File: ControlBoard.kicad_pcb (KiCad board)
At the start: 2 copper layers, 60 x 60 mm, 41 parts, among them J1 Conn_02x07_Odd_Even, J2 Conn_02x07_Odd_Even, J3 Conn_02x03_Odd_Even, J5 Conn_01x06, J6 Conn_01x06, J7 Conn_01x02, U1 STM32G473RCTx, U2 AT24CS02-XHM, U3 ICM-42668-P, U4 RT9013-33GB, U6 TLE9251VSJ

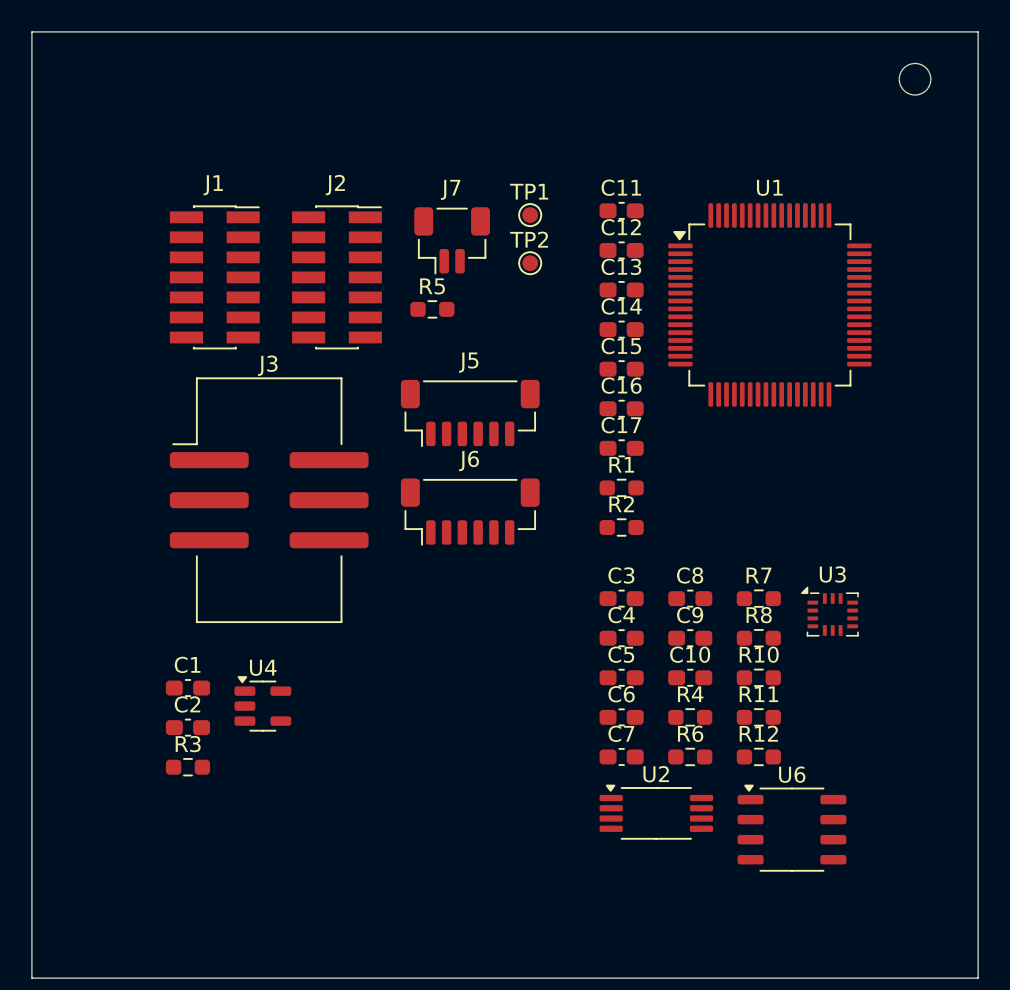
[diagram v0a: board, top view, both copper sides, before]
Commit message: 重新分配端子封装
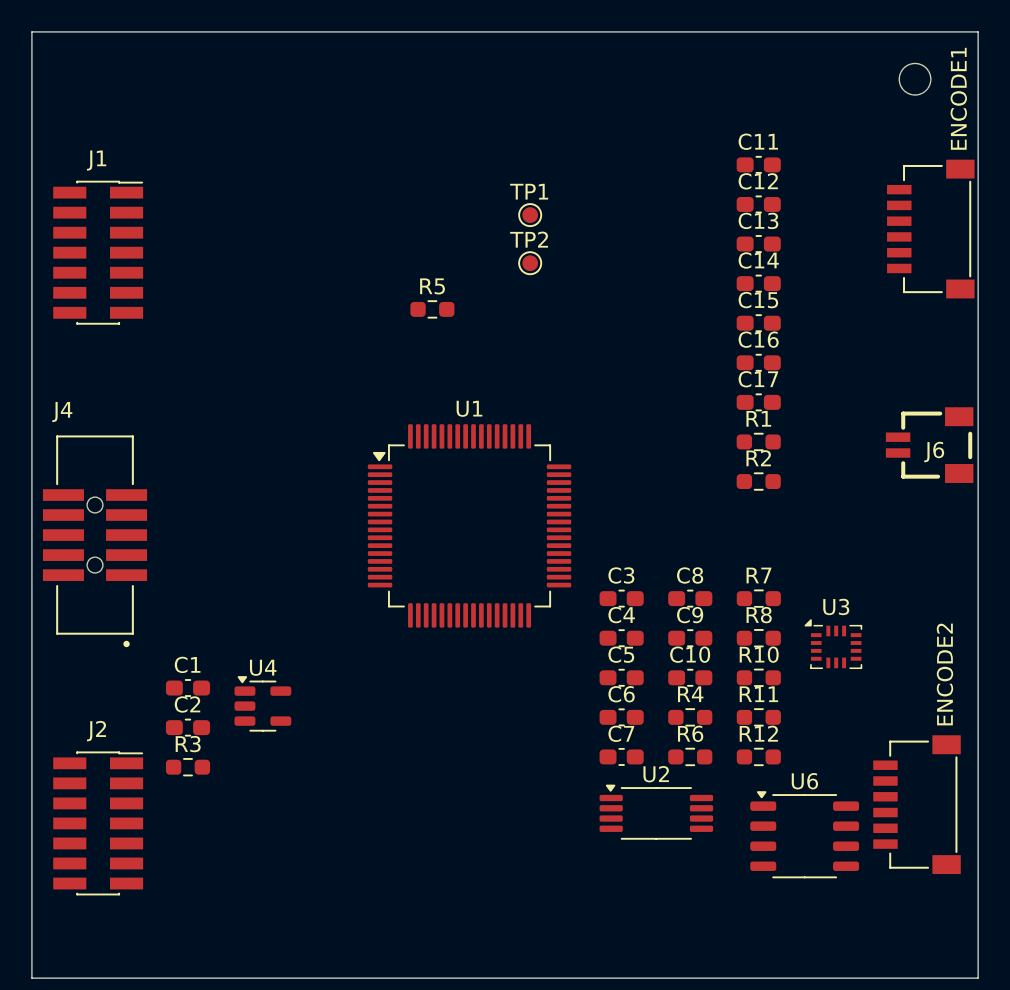
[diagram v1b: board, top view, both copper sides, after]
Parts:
- removed J3: Conn_02x03_Odd_Even, Connector_IDC:IDC-Header_2x03_P2.54mm_Vertical_SMD
- removed J5: Conn_01x06, Connector_JST:JST_SH_BM06B-SRSS-TB_1x06-1MP_P1.00mm_Vertical
- removed J7: Conn_01x02, Connector_JST:JST_SH_BM02B-SRSS-TB_1x02-1MP_P1.00mm_Vertical
- added ENCODE1: ENCODE1, footprints:JST_SH_BM06B-SRSS-TB_1x06-1MP_P1.00mm_Horizontal, F.Cu at (215.0, 70.5)
- added ENCODE2: Conn_01x06_MountingPin, footprints:JST_SH_BM06B-SRSS-TB_1x06-1MP_P1.00mm_Horizontal, F.Cu at (214.1, 107.0)
- added J4: Conn_02x05_Odd_Even, footprints:Box_Head_1.27mm_SMD_Vertical_02x05, F.Cu at (164.0, 89.9)
- J6: value Conn_01x06 -> Conn_01x02_MountingPin; footprint Connector_JST:JST_SH_BM06B-SRSS-TB_1x06-1MP_P1.00mm_Vertical -> footprints:JST_SH_BM02B-SRSS-TB_1x02-1MP_P1.00mm_Horizontal
- moved J2 37.8 mm to (164.2, 108.2)
- moved J6 29.4 mm to (216.9, 84.2), turned to 90 degrees
- moved U1 23.6 mm to (187.8, 89.3)
- moved C12 9.17 mm to (206.1, 68.9)
- moved C14 9.17 mm to (206.1, 74.0)
- moved C15 9.17 mm to (206.1, 76.5)
- moved C17 9.17 mm to (206.1, 81.5)
- moved R1 9.17 mm to (206.1, 84.0)
- moved C11 9.17 mm to (206.1, 66.4)
- moved C13 9.17 mm to (206.1, 71.5)
- moved C16 9.17 mm to (206.1, 79.0)
- moved R2 9.17 mm to (206.1, 86.5)
- moved J1 7.56 mm to (164.2, 72.0)
- moved U3 2.07 mm to (211.0, 97.0)
- moved U6 0.91 mm to (209.0, 109.0)
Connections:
- J6 pad 1: /3.3V -> /CAN_H
- J6 pad 2: /SPI3_CLK -> /CAN_L
- J6 pad MP: (no net) -> GND
- U1 pad 18: /SPI1_CS -> /MOTOR1_ENCODE_CS
- U1 pad 19: /SPI1_CLK -> /MOTOR1_ENCODE_CLK
- U1 pad 20: /SPI1_MISO -> /MOTOR1_ENCODE_MISO
- U1 pad 21: /SPI1_MOSI -> /MOTOR1_ENCODE_MOSI
- U1 pad 51: /SPI3_CS -> /MOTOR2_ENCODE_CS
- U1 pad 52: /SPI3_CLK -> /MOTOR2_ENCODE_CLK
- U1 pad 53: /SPI3_MISO -> /MOTOR2_ENCODE_MISO
- U1 pad 54: /SPI3_MOSI -> /MOTOR2_ENCODE_MOSI

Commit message: 修改板框
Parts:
- moved J2 91.9 mm to (73.0, 97.0)
- moved J4 91.3 mm to (73.0, 82.0)
- moved J1 91.3 mm to (73.0, 67.0)
- moved C1 76.9 mm to (93.1, 94.8)
- moved C2 76.9 mm to (93.1, 97.3)
- moved C3 76.9 mm to (120.6, 89.1)
- moved C4 76.9 mm to (120.6, 91.6)
- moved C5 76.9 mm to (120.6, 94.1)
- moved C6 76.9 mm to (120.6, 96.6)
- moved C7 76.9 mm to (120.6, 99.2)
- moved R3 76.9 mm to (93.1, 99.8)
- moved R5 76.9 mm to (108.6, 70.8)
- moved U4 76.9 mm to (97.9, 95.9)
- moved C10 76.9 mm to (125.0, 94.1)
- moved C11 76.9 mm to (129.3, 61.6)
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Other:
- board size 60 x 60 mm -> 80 x 60 mm

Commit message: PCB初布局
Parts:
- added C18: 22pF, Capacitor_SMD:C_0603_1608Metric_Pad1.08x0.95mm_HandSolder, F.Cu at (120.4, 85.6)
- added C19: 22pF, Capacitor_SMD:C_0603_1608Metric_Pad1.08x0.95mm_HandSolder, F.Cu at (120.1, 81.5)
- added C20: 0.1uF, Capacitor_SMD:C_0603_1608Metric_Pad1.08x0.95mm_HandSolder, F.Cu at (120.4, 75.2)
- added R9: 10K, Resistor_SMD:R_0603_1608Metric_Pad0.98x0.95mm_HandSolder, F.Cu at (118.8, 75.2)
- added SW1: SW_Push, Button_Switch_SMD:SW_SPST_CK_RS282G05A3, F.Cu at (127.0, 74.9)
- added Y1: 12MHz, Crystal:Crystal_SMD_3225-4Pin_3.2x2.5mm, F.Cu at (118.1, 83.6)
- moved C13 40.5 mm to (94.7, 87.7), turned to -90 degrees
- moved ENCODE2 34.5 mm to (142.8, 68.1)
- moved TP1 32.2 mm to (90.0, 85.3), turned to 180 degrees
- moved ENCODE1 30.7 mm to (142.8, 96.0)
- moved U3 29.5 mm to (105.7, 99.6)
- moved TP2 28.7 mm to (90.0, 82.3), turned to 180 degrees
- moved C12 28.4 mm to (101.6, 70.0)
- moved R5 26.7 mm to (84.5, 82.0), turned to 180 degrees
- moved C16 26.6 mm to (109.0, 91.2)
- moved C17 25.2 mm to (105.0, 70.0)
- moved R1 24.5 mm to (109.0, 92.8), turned to 180 degrees
- moved C15 24.3 mm to (105.0, 71.5)
- moved C14 24.1 mm to (113.2, 87.0), turned to -90 degrees
- moved R2 23.9 mm to (109.0, 94.3), turned to 180 degrees
- moved U6 22.2 mm to (131.3, 82.0)
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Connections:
- U1 pad 5: unconnected-(U1-PF0-Pad5) -> Net-(U1-PF0)
- U1 pad 6: unconnected-(U1-PF1-Pad6) -> Net-(U1-PF1)
- U1 pad 7: unconnected-(U1-PG10-Pad7) -> Net-(U1-PG10)
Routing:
- net Net-(U1-PF1): track 0.00 -> 11.0 mm
- net Net-(U3-AP_CS): track 0.00 -> 11.0 mm
- net Net-(U1-PF0): track 0.00 -> 11.0 mm
- net /MCU_Part/Peripheral/24C02_SDA: track 0.00 -> 8.45 mm
- net /MCU_Part/Peripheral/24C02_SCL: track 0.00 -> 6.54 mm
- net Net-(U6-STB): track 0.00 -> 3.54 mm
- net Net-(U2-WP): track 0.00 -> 3.24 mm
- net /MCU_Part/Peripheral/PB6_FDCAN2_TX: track 0.00 -> 3.17 mm
- net Net-(U6-CAN_H): track 0.00 -> 2.93 mm
- net /MCU_Part/Peripheral/PB11_FDCAN2_RX: track 0.00 -> 2.87 mm
- net Net-(U6-CAN_L): track 0.00 -> 2.82 mm
- net Net-(U3-INT2/FSYNC/CLKIN): track 0.00 -> 2.75 mm
- net /CAN_L: track 0.00 -> 2.20 mm
- net /CAN_H: track 0.00 -> 2.20 mm

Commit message: 增加测试点
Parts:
- added TP10: TestPoint_Small, TestPoint:TestPoint_Pad_D1.0mm, F.Cu at (156.2, 87.4)
- added TP11: TestPoint_Small, TestPoint:TestPoint_Pad_D1.0mm, F.Cu at (156.2, 90.4)
- added TP12: TestPoint_Small, TestPoint:TestPoint_Pad_D1.0mm, F.Cu at (156.2, 93.5)
- added TP13: TestPoint_Small, TestPoint:TestPoint_Pad_D1.0mm, F.Cu at (159.3, 72.1)
- added TP14: TestPoint_Small, TestPoint:TestPoint_Pad_D1.0mm, F.Cu at (159.3, 75.2)
- added TP15: TestPoint_Small, TestPoint:TestPoint_Pad_D1.0mm, F.Cu at (159.3, 78.2)
- added TP16: TestPoint_Small, TestPoint:TestPoint_Pad_D1.0mm, F.Cu at (159.3, 81.3)
- added TP17: TestPoint_Small, TestPoint:TestPoint_Pad_D1.0mm, F.Cu at (159.3, 84.3)
- added TP18: TestPoint_Small, TestPoint:TestPoint_Pad_D1.0mm, F.Cu at (159.3, 87.4)
- added TP19: TestPoint_Small, TestPoint:TestPoint_Pad_D1.0mm, F.Cu at (159.3, 90.4)
- added TP20: TestPoint_Small, TestPoint:TestPoint_Pad_D1.0mm, F.Cu at (159.3, 93.5)
- added TP21: TestPoint_Small, TestPoint:TestPoint_Pad_D1.0mm, F.Cu at (162.3, 72.1)
- added TP22: TestPoint_Small, TestPoint:TestPoint_Pad_D1.0mm, F.Cu at (162.3, 75.2)
- added TP23: TestPoint_Small, TestPoint:TestPoint_Pad_D1.0mm, F.Cu at (162.3, 78.2)
- added TP24: TestPoint_Small, TestPoint:TestPoint_Pad_D1.0mm, F.Cu at (162.3, 81.3)
- added TP25: TestPoint_Small, TestPoint:TestPoint_Pad_D1.0mm, F.Cu at (162.3, 84.3)
- added TP26: TestPoint_Small, TestPoint:TestPoint_Pad_D1.0mm, B.Cu at (93.3, 79.3)
- added TP27: TestPoint_Small, TestPoint:TestPoint_Pad_D1.0mm, F.Cu at (162.3, 90.4)
- added TP28: TestPoint_Small, TestPoint:TestPoint_Pad_D1.0mm, F.Cu at (162.3, 93.5)
- added TP29: TestPoint_Small, TestPoint:TestPoint_Pad_D1.0mm, F.Cu at (165.4, 72.1)
- added TP3: TestPoint_Small, TestPoint:TestPoint_Pad_D1.0mm, F.Cu at (140.7, 78.4)
- added TP30: TestPoint_Small, TestPoint:TestPoint_Pad_D1.0mm, F.Cu at (165.4, 75.2)
- added TP31: TestPoint_Small, TestPoint:TestPoint_Pad_D1.0mm, F.Cu at (165.4, 78.2)
- added TP32: TestPoint_Small, TestPoint:TestPoint_Pad_D1.0mm, F.Cu at (165.4, 81.3)
- added TP33: TestPoint_Small, TestPoint:TestPoint_Pad_D1.0mm, F.Cu at (165.4, 84.3)
- added TP34: TestPoint_Small, TestPoint:TestPoint_Pad_D1.0mm, F.Cu at (165.4, 87.4)
- added TP35: TestPoint_Small, TestPoint:TestPoint_Pad_D1.0mm, F.Cu at (165.4, 90.4)
- added TP36: TestPoint_Small, TestPoint:TestPoint_Pad_D1.0mm, F.Cu at (165.4, 93.5)
- added TP37: TestPoint_Small, TestPoint:TestPoint_Pad_D1.0mm, F.Cu at (168.4, 72.1)
- added TP38: TestPoint_Small, TestPoint:TestPoint_Pad_D1.0mm, F.Cu at (168.4, 75.2)
- added TP39: TestPoint_Small, TestPoint:TestPoint_Pad_D1.0mm, F.Cu at (168.4, 78.2)
- added TP4: TestPoint_Small, TestPoint:TestPoint_Pad_D1.0mm, F.Cu at (140.7, 86.6)
- added TP40: TestPoint_Small, TestPoint:TestPoint_Pad_D1.0mm, F.Cu at (168.4, 81.3)
- added TP41: TestPoint_Small, TestPoint:TestPoint_Pad_D1.0mm, F.Cu at (168.4, 84.3)
- added TP42: TestPoint_Small, TestPoint:TestPoint_Pad_D1.0mm, F.Cu at (168.4, 87.4)
- added TP43: TestPoint_Small, TestPoint:TestPoint_Pad_D1.0mm, F.Cu at (168.4, 90.4)
- added TP44: TestPoint_Small, TestPoint:TestPoint_Pad_D1.0mm, F.Cu at (168.4, 93.5)
- added TP45: TestPoint_Small, TestPoint:TestPoint_Pad_D1.0mm, F.Cu at (171.5, 72.1)
- added TP46: TestPoint_Small, TestPoint:TestPoint_Pad_D1.0mm, F.Cu at (171.5, 75.2)
- added TP47: TestPoint_Small, TestPoint:TestPoint_Pad_D1.0mm, F.Cu at (171.5, 78.2)
- added TP48: TestPoint_Small, TestPoint:TestPoint_Pad_D1.0mm, F.Cu at (171.5, 81.3)
- added TP5: TestPoint_Small, TestPoint:TestPoint_Pad_D1.0mm, F.Cu at (156.2, 72.1)
- added TP6: TestPoint_Small, TestPoint:TestPoint_Pad_D1.0mm, F.Cu at (156.2, 75.2)
- added TP7: TestPoint_Small, TestPoint:TestPoint_Pad_D1.0mm, F.Cu at (156.2, 78.2)
- added TP8: TestPoint_Small, TestPoint:TestPoint_Pad_D1.0mm, F.Cu at (156.2, 81.3)
- added TP9: TestPoint_Small, TestPoint:TestPoint_Pad_D1.0mm, F.Cu at (156.2, 84.3)
- moved C19 7.11 mm to (120.1, 88.6), turned to 45 degrees
- moved C18 5.44 mm to (116.1, 88.9), turned to -45 degrees
- moved C13 4.74 mm to (90.2, 88.9)
- moved Y1 3.05 mm to (118.1, 86.6), turned to -135 degrees
- moved U1 2.67 mm to (101.5, 82.0)
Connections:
- J6 pad 1: /CAN_H -> /CAN_L
- J6 pad 2: /CAN_L -> /CAN_H
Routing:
- net /MCU_Part/Peripheral/24C02_SDA: track 8.45 -> 2.35 mm
- net Net-(U1-PF1): track 11.0 -> 6.28 mm
- net Net-(U1-PF0): track 11.0 -> 6.26 mm
- net /MCU_Part/Peripheral/24C02_SCL: track 6.54 -> 1.84 mm
- net +5V: track 0.00 -> 2.98 mm
- net /CAN_H: track 2.20 -> 4.73 mm
- net /CAN_L: track 2.20 -> 4.70 mm
- net /MOTOR1_U-: track 0.00 -> 2.45 mm, vias 0 -> 1

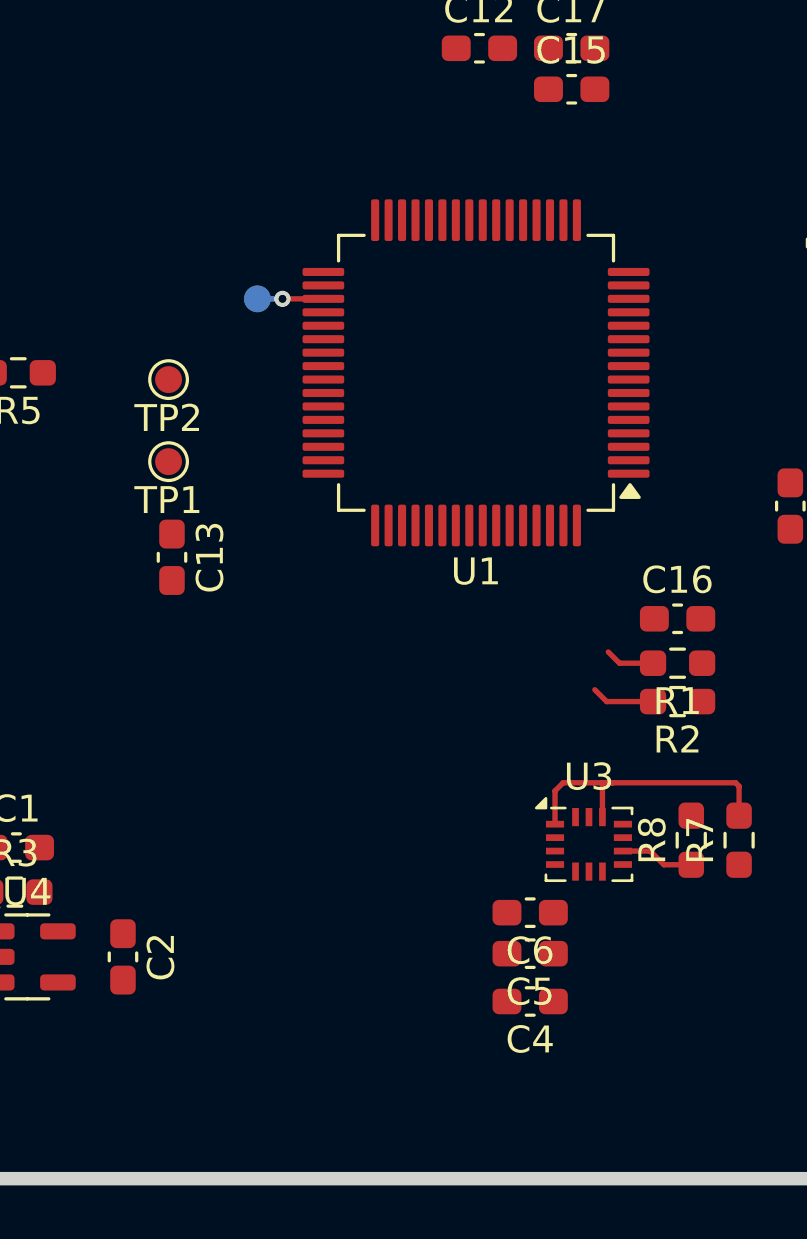
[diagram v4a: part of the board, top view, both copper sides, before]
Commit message: 优化Type-C电路
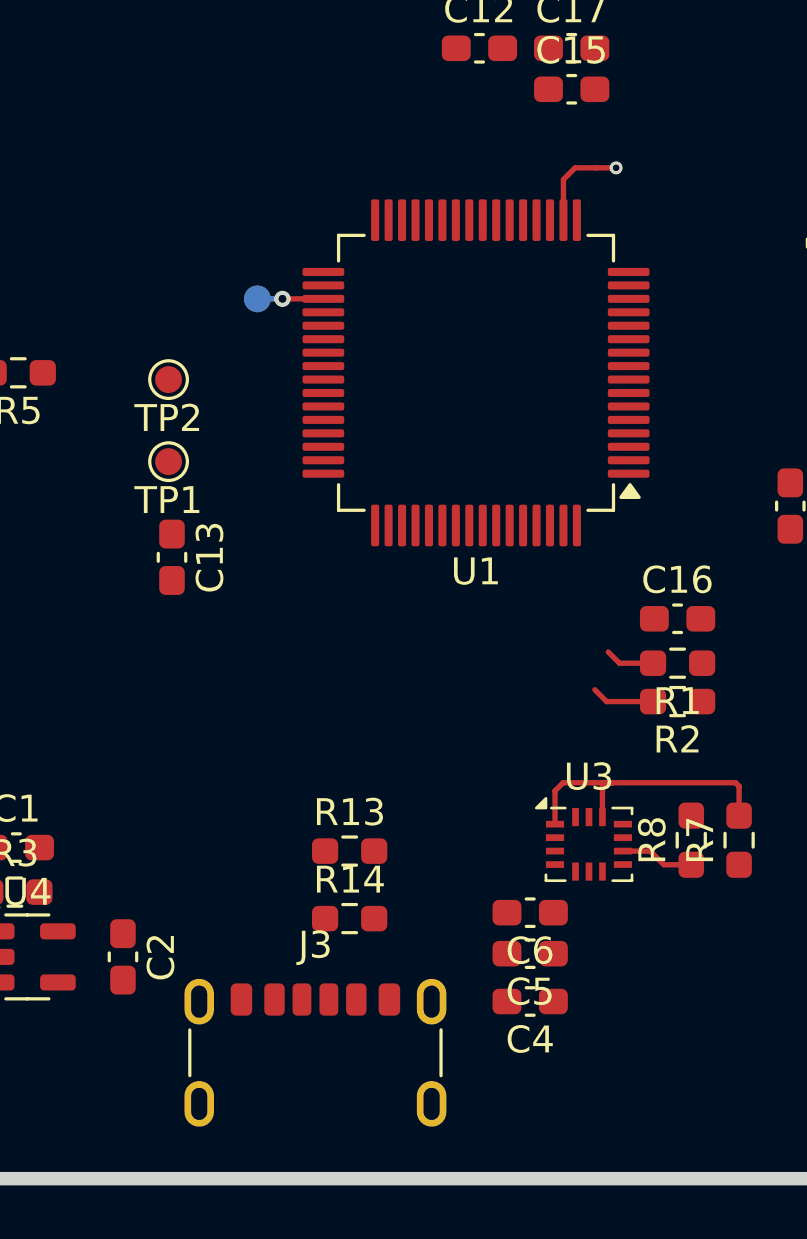
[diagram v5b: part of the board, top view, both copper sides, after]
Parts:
- added J3: USB_C_Receptacle_PowerOnly_6P, Connector_USB:USB_C_Receptacle_GCT_USB4125-xx-x-0190_6P_TopMnt_Horizontal, F.Cu at (95.5, 108.4)
- added R13: 10K, Resistor_SMD:R_0603_1608Metric_Pad0.98x0.95mm_HandSolder, F.Cu at (96.8, 99.8)
- added R14: 10K, Resistor_SMD:R_0603_1608Metric_Pad0.98x0.95mm_HandSolder, F.Cu at (96.8, 102.3)
- Y1: value 12MHz -> 32MHz
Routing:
- net /MOTOR1_ENCODE_CS: track 0.00 -> 3.65 mm, vias 0 -> 1

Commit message: 优化布局20250919
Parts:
- TP1, TP10, TP11, TP12, TP13, TP14, TP15, TP16, TP17, TP18, TP19, TP2, TP20, TP21, TP22, TP23, TP24, TP25, TP27, TP28, TP29, TP3, TP30, TP31, TP32, TP33, TP34, TP35, TP36, TP37, TP38, TP39, TP4, TP40, TP41, TP42, TP43, TP44, TP45, TP46, TP47, TP48, TP5, TP6, TP7, TP8, TP9: moved to B.Cu
- moved SW1 38.7 mm to (108.6, 109.0), turned to 0 degrees
- moved C20 32.0 mm to (111.8, 106.0), turned to 180 degrees
- moved R6 30.0 mm to (96.3, 97.8), turned to 180 degrees
- moved R9 30.0 mm to (111.8, 104.4), turned to 0 degrees
- moved C4 28.1 mm to (121.6, 83.9), turned to 0 degrees
- moved C3 27.6 mm to (96.3, 99.3), turned to 180 degrees
- moved TP5 27.4 mm to (183.6, 70.9), turned to 180 degrees
- moved C6 26.8 mm to (121.6, 82.4), turned to 0 degrees
- moved C14 23.5 mm to (95.1, 72.0), turned to 90 degrees
- moved C5 22.7 mm to (117.2, 85.5), turned to 0 degrees
- moved C17 22.7 mm to (104.6, 92.7), turned to -90 degrees
- moved R7 22.6 mm to (121.6, 79.3), turned to 180 degrees
- moved R8 22.1 mm to (121.6, 80.9), turned to 0 degrees
- moved C16 21.8 mm to (98.6, 72.0), turned to 90 degrees
- moved C15 21.3 mm to (102.9, 92.7), turned to -90 degrees
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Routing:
- net GND: track 0.00 -> 77.3 mm, vias 0 -> 47
- net +3.3V: track 0.00 -> 45.6 mm
- net /MCU_Part/Peripheral/ICM-20602-INT: track 0.00 -> 33.7 mm, vias 0 -> 2
- net /MCU_Part/Peripheral/24C02_SDA: track 2.35 -> 27.5 mm, vias 0 -> 2
- net /MCU_Part/Peripheral/24C02_SCL: track 1.84 -> 25.1 mm, vias 0 -> 2
- net Net-(U1-PF1): track 6.28 -> 13.0 mm
- net Net-(U1-PG10): track 0.00 -> 4.69 mm
- net Net-(U1-PF0): track 6.26 -> 10.5 mm
- net Net-(J4-Pin_5): track 0.00 -> 3.91 mm
- net /MOTOR1_ENCODE_CS: track 3.65 -> 0.00 mm, vias 1 -> 0
- net Net-(J3-CC2): track 0.00 -> 3.60 mm
- net Net-(J3-CC1): track 0.00 -> 3.33 mm
- net /MOTOR2_U-: track 0.00 -> 3.15 mm, vias 0 -> 2
- net /MOTOR2_V-: track 0.00 -> 2.08 mm, vias 0 -> 1
- net /MOTOR2_ENCODE_MISO: track 0.00 -> 2.08 mm, vias 0 -> 1
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
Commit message: 优化PCB布线20250919
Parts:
- added C21: 0.1uF, Capacitor_SMD:C_0603_1608Metric_Pad1.08x0.95mm_HandSolder, F.Cu at (123.4, 105.8)
- added R15: 10K, Resistor_SMD:R_0603_1608Metric_Pad0.98x0.95mm_HandSolder, F.Cu at (123.4, 104.1)
- added SW2: SW_Push, Button_Switch_SMD:SW_SPST_CK_RS282G05A3, F.Cu at (120.1, 108.8)
- moved TP33 121.8 mm to (59.2, 100.4)
- moved TP46 119.7 mm to (65.4, 93.2)
- moved TP29 117.7 mm to (51.9, 64.2)
- moved TP41 115.9 mm to (65.4, 99.1)
- moved TP18 115.5 mm to (57.8, 67.8)
- moved TP25 114.7 mm to (51.9, 73.7)
- moved TP27 114.2 mm to (51.9, 83.3)
- moved TP28 114.1 mm to (51.9, 88.1)
- moved TP43 112.5 mm to (65.4, 107.8)
- moved TP17 112.0 mm to (57.8, 72.0)
- moved TP14 111.9 mm to (57.8, 65.7)
- moved TP15 111.9 mm to (57.8, 69.9)
- moved TP16 111.8 mm to (57.8, 74.0)
- moved TP21 111.7 mm to (61.0, 63.3)
- moved TP19 109.5 mm to (61.0, 69.6)
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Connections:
- J1 pad 12: /MOTOR1_U- -> /MOTOR1_W-
- J2 pad 12: /MOTOR2_U- -> /MOTOR2_W-
- TP18 pad 1: /MOTOR1_U- -> /MOTOR1_W-
- TP30 pad 1: /MOTOR1_U- -> /MOTOR1_W-
- TP36 pad 1: /MOTOR2_U- -> /MOTOR2_W-
- TP46 pad 1: /MOTOR2_U- -> /MOTOR2_W-
- U1 pad 2: unconnected-(U1-PC13-Pad2) -> Net-(U1-PC13)
- U1 pad 37: /MOTOR1_U- -> /MOTOR1_W-
- U1 pad 58: /MOTOR2_U- -> /MOTOR2_W-
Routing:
- net /MOTOR2_ADC_U: track 0.00 -> 65.2 mm, vias 0 -> 2
- net /MOTOR2_ADC_V: track 0.00 -> 62.3 mm, vias 0 -> 2
- net /MOTOR2_ADC_W: track 0.00 -> 59.7 mm, vias 0 -> 2
- net /MOTOR2_ENCODE_CLK: track 1.58 -> 60.6 mm, vias 1 -> 2
- net /MOTOR2_ENCODE_CS: track 2.08 -> 60.2 mm, vias 1 -> 2
- net /MOTOR2_ENCODE_MOSI: track 1.58 -> 59.1 mm, vias 1 -> 2
- net /MOTOR2_ENCODE_MISO: track 2.08 -> 59.4 mm, vias 1 -> 2
- net /MOTOR1_ENCODE_CS: track 0.00 -> 56.8 mm, vias 0 -> 2
- net /MOTOR1_ADC_W: track 0.00 -> 56.3 mm, vias 0 -> 2
- net /MOTOR1_ADC_U: track 0.00 -> 56.2 mm, vias 0 -> 2
- net /MOTOR1_ADC_V: track 0.00 -> 56.2 mm, vias 0 -> 2
- net /MOTOR1_ENCODE_CLK: track 0.00 -> 55.6 mm, vias 0 -> 1
- net /MOTOR1_ENCODE_MOSI: track 0.00 -> 55.0 mm, vias 0 -> 1
- net /MOTOR1_ENCODE_MISO: track 0.00 -> 54.0 mm, vias 0 -> 2
- net /MOTOR2_W-: track 0.00 -> 46.8 mm, vias 0 -> 1
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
